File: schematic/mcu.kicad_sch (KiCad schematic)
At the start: 32 parts, among them J2 USB4105-xx-A, J4 1WIRE, J5 1WIRE, J6 1WIRE, J7 1WIRE, U1 ESP32-C6-MINI-1-N4, U4 USBLC6-2SC6, U5 TMP1075D

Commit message: Assign LCSC part numbers, mark PS1 DNP for JLC assembly
Every BOM line except PS1 now carries an LCSC field. Generic passives
move to JLC basic parts with equal or better ratings. Parts not stocked
at LCSC are swapped: C1/C2 to T520D227M010ATE018 (10 V), F1 to
0805L035/24XR, J8 to a generic gold 2x6 header, D6 to SMF3.3A.
PS1 (Ag9905MT) is DNP: bought separately and hand-soldered.
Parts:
- C12: LCSC (none) -> C15850
- C13, C15: LCSC (none) -> C1525; MANUFACTURER YAGEO -> Samsung Electro-Mechanics; MPN CC0402KRX7R7BB104 -> CL05B104KO5NNNC
- C14: LCSC (none) -> C15849; MPN CL10A105KO8NNNC -> CL10A105KB8NNNC
- D4: LCSC (none) -> C5246833
- D5: LCSC (none) -> C82326
- J2: LCSC (none) -> C3020560
- J4, J5, J6, J7: LCSC (none) -> C131339
- R13, R14, R30, R5, R6: LCSC (none) -> C25900; MANUFACTURER YAGEO -> UNI-ROYAL; MPN RC0402FR-074K7L -> 0402WGF4701TCE
- R19, R27, R7: LCSC (none) -> C25744
- R24, R25: LCSC (none) -> C25905; MANUFACTURER YAGEO -> UNI-ROYAL; MPN RC0402FR-075K1L -> 0402WGF5101TCE
- R34, R35: LCSC (none) -> C25092; MANUFACTURER YAGEO -> UNI-ROYAL; MPN RC0402FR-0722RL -> 0402WGF220JTCE
- R36: LCSC (none) -> C22775; MANUFACTURER YAGEO -> UNI-ROYAL; MPN RC0603FR-07100RL -> 0603WAF1000T5E
- R8: LCSC (none) -> C11702; MANUFACTURER YAGEO -> UNI-ROYAL; MPN RC0402FR-071KL -> 0402WGF1001TCE
- U1: LCSC (none) -> C5736265
- U4: LCSC (none) -> C7519
- U5: LCSC (none) -> C2878381

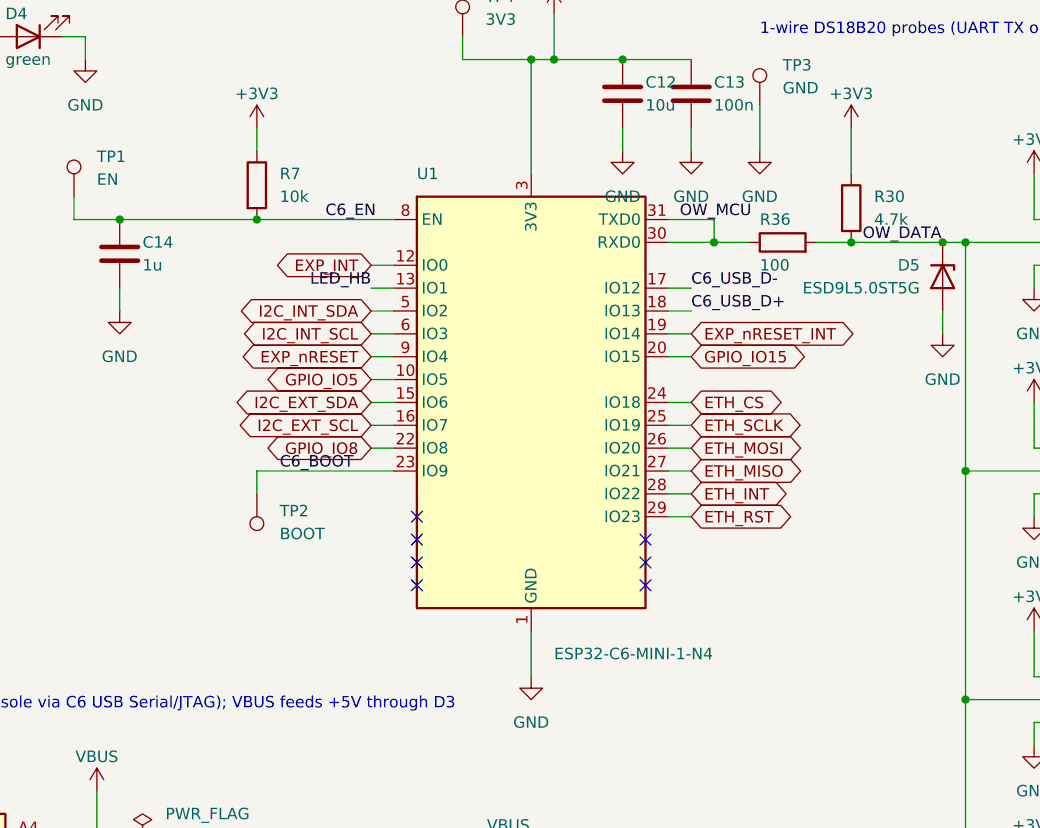
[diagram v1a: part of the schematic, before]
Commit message: WROOM-1-N8, node power sensing, dry contacts, I2C port, VIN sense
- U1 ESP32-C6-MINI-1-N4 -> ESP32-C6-WROOM-1-N8 (8 MB for two OTA
  slots; N16 is a drop-in). Project-local symbol and footprint from the
  datasheet. GPIO14 is not on the WROOM: EXP_nRESET_INT moves to
  GPIO10; GPIO11 spare.
- Node connectors J11-J18 go to JST PH 5p: PWR_SW, RST_SW, node GND,
  PLED+, PLED-. PLED drives 2x TLP290-4 AC-input optos; 10k pull-ups
  -> U15 MCP23017 @0x21 GPA0-7 (NODE_ON1-8).
- U15 GPB0-3: 4 dry-contact inputs (J10, RC + TPD4E05U06 ESD).
- J9 I2C sensor port (JST PH 4p, Qwiic order) on the protected header bus.
- VIN_SENSE 100k/10k divider to GPIO5 (ADC); J8 pin 9 now unused.
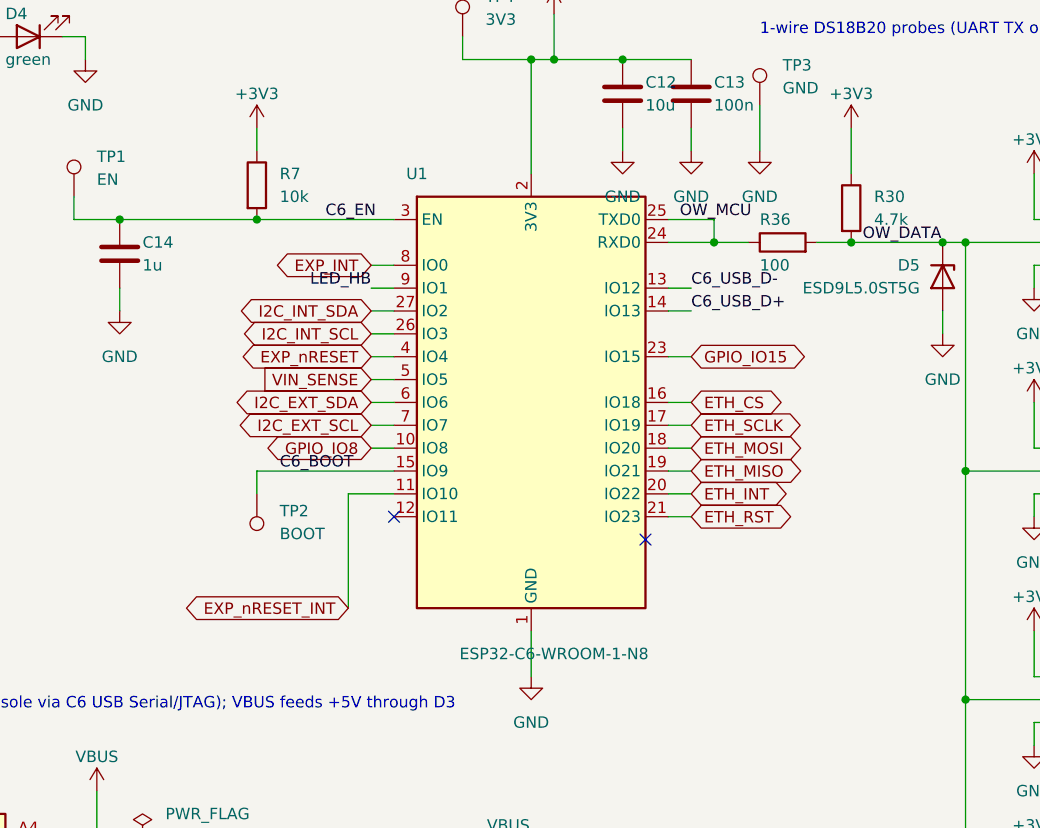
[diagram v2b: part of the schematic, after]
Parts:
- removed U1: ESP32-C6-MINI-1-N4, RF_Module:ESP32-C6-MINI-1, symbol RF_Module:ESP32-C6-MINI-1
- added U1: ESP32-C6-WROOM-1-N8, granite:ESP32-C6-WROOM-1, symbol granite:ESP32-C6-WROOM-1
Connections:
- net +3V3: now also U1.2 (3V3)
- net C6_BOOT: now also U1.15 (IO9)
- net C6_EN: now also U1.3 (EN)
- net C6_USB_D+: now also U1.14 (IO13)
- net C6_USB_D-: now also U1.13 (IO12)
- net ETH_CS: now also U1.16 (IO18)
- net ETH_INT: now also U1.20 (IO22)
- net ETH_MISO: now also U1.19 (IO21)
- net ETH_MOSI: now also U1.18 (IO20)
- net ETH_RST: now also U1.21 (IO23)
- net ETH_SCLK: now also U1.17 (IO19)
- net EXP_INT: now also U1.8 (IO0)
- net EXP_nRESET: now also U1.4 (IO4)
- net EXP_nRESET_INT: now also U1.11 (IO10)
- net GND: now also U1.1 (GND), U1.28 (GND), U1.29 (GND)
- net GPIO_IO15: now also U1.23 (IO15)
- net GPIO_IO8: now also U1.10 (IO8)
- net I2C_EXT_SCL: now also U1.7 (IO7)
- net I2C_EXT_SDA: now also U1.6 (IO6)
- net I2C_INT_SCL: now also U1.26 (IO3)
- net I2C_INT_SDA: now also U1.27 (IO2)
- net LED_HB: now also U1.9 (IO1)
- net OW_MCU: now also U1.24 (RXD0), U1.25 (TXD0)
- new net VIN_SENSE: U1.5 (IO5)
- no-connect marks 10 -> 5

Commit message: J2: GCT USB4105-GF-A -> HRO TYPE-C-31-M-12 (C165948)
The GCT part is down to 140 at JLC. The HRO footprint has the same pins,
pegs and shield slots (within 0.03 mm) but 1.45 mm signal pads that reach
0.5 mm further in, onto the old rear fan-out.

Rear escapes laid by script: D+ join at y 37.35, CC1/CC2 straight back,
VBUS left pair to the front via, right pair to a rear via with a 0.5 mm
B.Cu link under the body. KRT (krt_reroute.sh --keep) routed D+, CC1,
CC2 and I2C_EXT_SDA from there; the SDA via it put in U1 pad 6 moved to
(125.0, 70.0). J2 silk outline dropped (edge part, clashed with the
shield pads at 0.15 mm), GND pads solid to the pour.

tools/krt_reroute.sh: --keep routes from existing copper instead of
clearing it; signal pass now uses the power-net widths of krt_route.sh.
tools/jlcfab.py: centroid offset for the HRO footprint (0, -1.424).

ERC 0; DRC 0 unconnected, 0 parity, the 3 known violations plus the
J2-differs-from-library warning.
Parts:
- J2: value USB4105-xx-A -> TYPE-C-31-M-12; footprint Connector_USB:USB_C_Receptacle_GCT_USB4105-xx-A_16P_TopMnt_Horizontal -> Connector_USB:USB_C_Receptacle_HRO_TYPE-C-31-M-12; LCSC C3020560 -> C165948; MANUFACTURER Global Connector Technology -> Korean Hroparts Elec; MPN USB4105-GF-A -> TYPE-C-31-M-12
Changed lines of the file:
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@@
 			)
 		)
-		(property "Value" "USB4105-xx-A"
+		(property "Value" "TYPE-C-31-M-12"
 			(at 45.72 191.77 0)
 			(show_name no)
@@
 			)
 		)
-		(property "Footprint" "Connector_USB:USB_C_Receptacle_GCT_USB4105-xx-A_16P_TopMnt_Horizontal"
+		(property "Footprint" "Connector_USB:USB_C_Receptacle_HRO_TYPE-C-31-M-12"
 			(at 40.64 165.1 0)
 			(hide yes)
@@
 			)
 		)
-		(property "MANUFACTURER" "Global Connector Technology"
+		(property "MANUFACTURER" "Korean Hroparts Elec"
 			(at 40.64 165.1 0)
 			(hide yes)
@@
 			)
 		)
-		(property "MPN" "USB4105-GF-A"
+		(property "MPN" "TYPE-C-31-M-12"
 			(at 40.64 165.1 0)
 			(hide yes)
@@
 			)
 		)
-		(property "LCSC" "C3020560"
+		(property "LCSC" "C165948"
 			(at 40.64 165.1 0)
 			(hide yes)
